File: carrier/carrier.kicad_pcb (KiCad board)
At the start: 4 copper layers, 9.2 x 7.4 mm, 2 parts, among them J1 DF40GB-30DP-0.4V(51), U1 TC58NVG1S3HBAI6

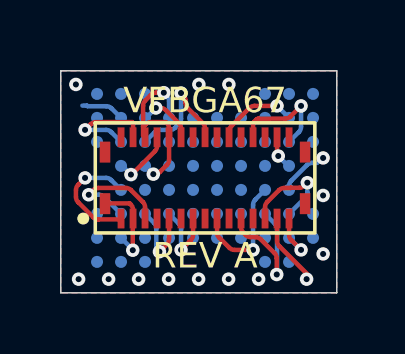
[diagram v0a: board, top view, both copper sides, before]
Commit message: Generate the JLCPCB rule set instead of hand-setting it
Read JLCPCB's capabilities page properly and turned it into something the
repo enforces rather than something a comment claims.

tools/jlc-4layer.kicad_dru holds the conditional constraints KiCad cannot
express as a global number (SMD-only, inner-layer-only, plated-only), and
tools/drc-rules.py pushes both those and the scalar limits into every
project. `make rules` applies, `make check` fails on drift. Every value is
quoted with the section it came from; see docs/jlc-rules.md.

What the old numbers had wrong:
  - base had KiCad's default 0.5 mm copper-to-edge; JLC allows 0.2
  - min_silk_clearance 0, text height 0.8, text thickness 0.08 were all
    below JLC's legend minimums, so bad silkscreen passed silently
  - min_hole_clearance 0.25 was conservative; JLC's inner-layer via hole to
    copper is 0.20. The carrier gains margin it did not have when routed --
    the note says not to spend it, since 0.45/0.20 sits on the cost boundary
  - min_via_diameter 0.3 was neither JLC's floor (0.25) nor the cost
    boundary (0.45). Now the floor, with the boundary as a warning-severity
    rule so shrinking a via pad is visible without failing the build

Panel recipe was wrong in three ways against the same page: 0.45 mm bites
are under the 0.5 mm NPTH minimum, and a 3 mm frame meets the plain tooling
edge minimum but not the 5 mm one for mouse-bite breakaway. Now 0.5 mm bites
at 0.75 mm on a 5 mm frame, 56.80 x 49.60 mm, 16 up.

kikit treats bite spacing as a maximum and divides each cut evenly, so 0.75
lands as low as 0.667 and tab junctions double up within 0.13 mm. Culling
afterwards beats hunting for a spacing whose rounding happens to work: 160
hole_to_hole violations -> 0. Dropping max_error to 0.001 mm clears the 6
copper_edge_clearance hits, which were 0.5 um of arc faceting against the
millradius corners, not a real clearance problem.

Also: cross-checked the ball map against courk's NandBug, which targets t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
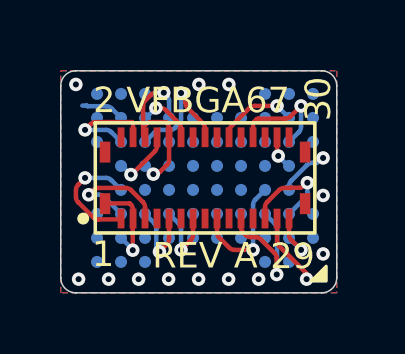
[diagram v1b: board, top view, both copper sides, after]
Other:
- outline, holes or cut-outs redrawn
- board text added: "1"
- board text added: "2"
- board text added: "29"
- board text added: "30"

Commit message: Regenerate the panel against Alex's second silk pass
Carrier silk warnings 20 -> 6: the four pin-number texts are gone and U1's
B.SilkS no longer runs off the board edge. What is left is REV A and
VFBGA67, still 0.85 mm / 0.106 mm against JLC's 1.0 / 0.15 legend minimum,
and both crossing J1's silk rectangle.

Panel: 56.80 x 49.60 mm, 16 up, 412 mouse bites, no hard violations.

Also fixed two cosmetic bugs in panelize.sh's own summary -- the board-count
match was missing the library nickname prefix so it always printed 0, and
the outline-extent regex required (layer "Edge.Cuts") at a fixed offset from
(start ...), which it is not, so the size line never printed. Neither
affected the panel itself.
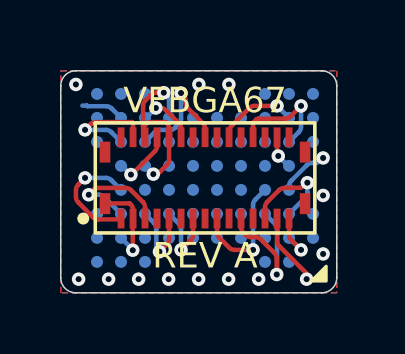
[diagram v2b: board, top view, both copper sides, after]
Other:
- board text removed: "1"
- board text removed: "2"
- board text removed: "29"
- board text removed: "30"
